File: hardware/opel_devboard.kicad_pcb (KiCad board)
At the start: 2 copper layers, 35 parts, among them P1 CONN_01X17, P2 CONN_01X06, P4 CONN_01X04, P5 CONN_01X04, SW1 SPST, SW2 SPST, U1 ISO1050, U2 LPC11C14, U3 MCP2515_TSSOP, U4 ISO1050, U5 MCP1755

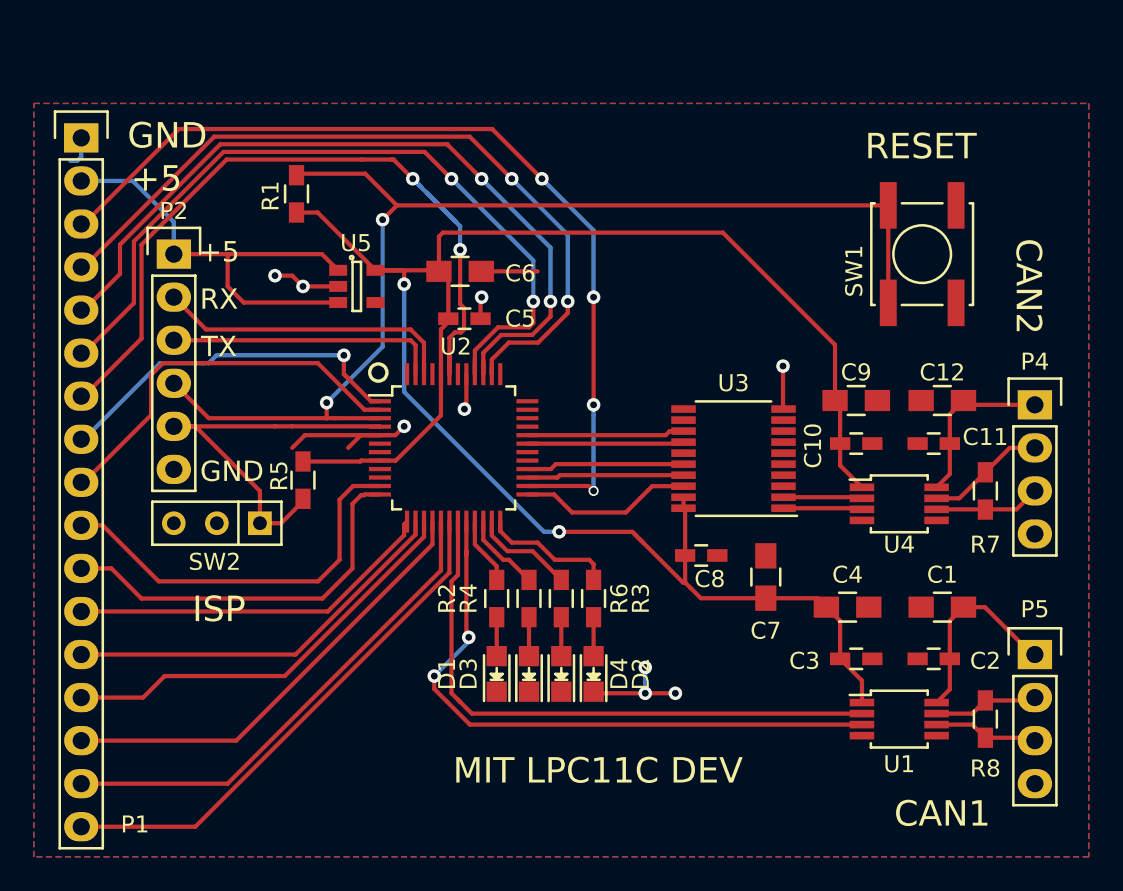
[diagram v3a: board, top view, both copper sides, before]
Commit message: devboard fixed, added LED, Added Capacitor, Changed CAN chips
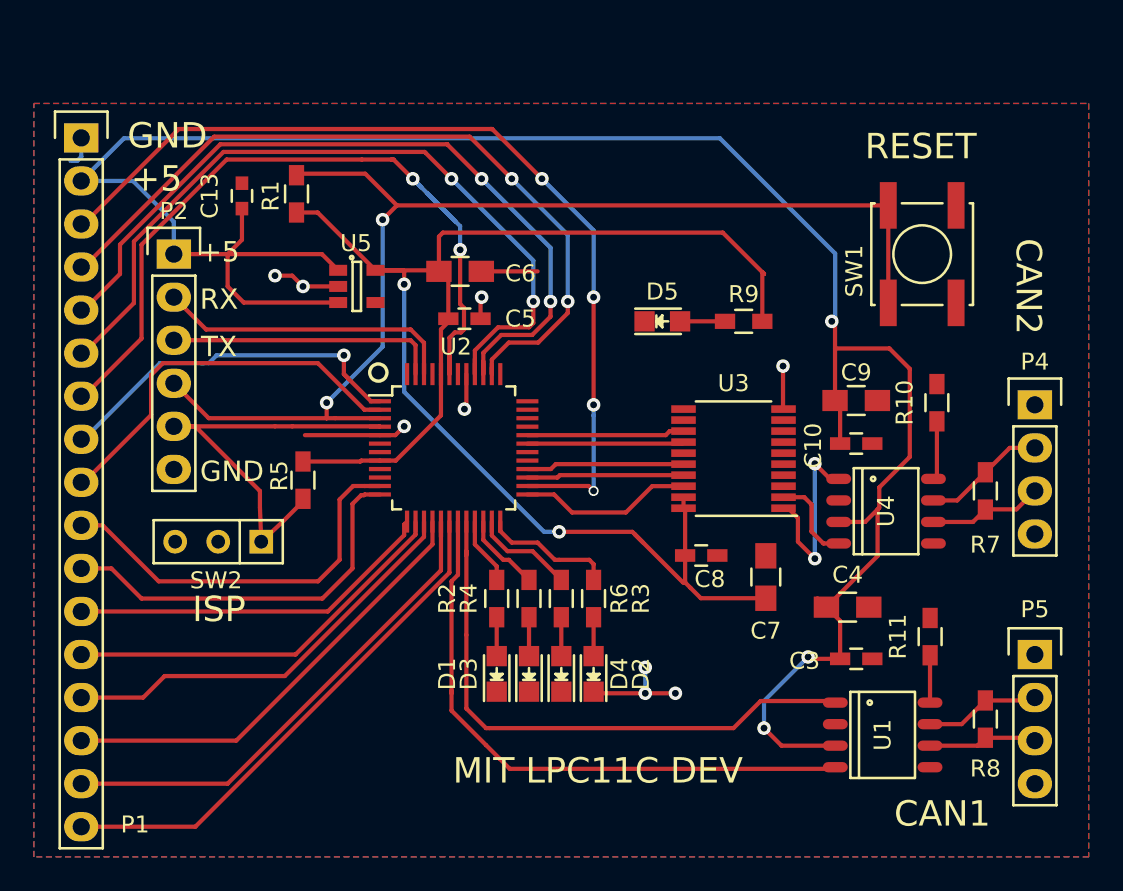
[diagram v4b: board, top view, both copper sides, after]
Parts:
- removed C1: 10uF, Capacitors_SMD:C_0805_HandSoldering
- removed C11, C2: 0.1uF, Capacitors_SMD:C_0603_HandSoldering
- removed C12: 1uF, Capacitors_SMD:C_0805_HandSoldering
- added C13: 1μF, Capacitors_SMD:C_0603, F.Cu at (165.9, 52.4)
- added D5: LED, LEDs:LED_0805, F.Cu at (190.7, 59.8)
- added R10: 20k, Resistors_SMD:R_0603_HandSoldering, F.Cu at (206.9, 64.6)
- added R11: 20k, Resistors_SMD:R_0603_HandSoldering, F.Cu at (206.5, 78.4)
- added R9: 200, Resistors_SMD:R_0603_HandSoldering, F.Cu at (195.5, 59.8)
- U1, U4: value ISO1050 -> MCP2551-I/SN; footprint Housings_SSOP:MSOP-8_3x3mm_Pitch0.65mm -> SO-8
- moved U1 1.35 mm to (203.7, 84.2), turned to 270 degrees
- moved SW2 1.09 mm to (164.5, 72.8)
- moved U4 0.89 mm to (203.9, 71.0), turned to 270 degrees
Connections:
- net GNDD renamed Net-(U1-Pad5)
- C10 pad 1: +3V3 -> +5V
- C3 pad 1: +3V3 -> +5V
- C4 pad 1: +3V3 -> +5V
- C9 pad 1: +3V3 -> +5V
- P4 pad 1: /Micro Controller/CAN2P -> /Output Connectors/CAN2P
- P5 pad 1: /Micro Controller/CAN1P -> /Output Connectors/CAN1P
- U1 pad 1: +3V3 -> Net-(U1-Pad1)
- U1 pad 2: Net-(U1-Pad2) -> GND
- U1 pad 3: Net-(U1-Pad3) -> +5V
- U1 pad 4: GND -> Net-(U1-Pad4)
- U1 pad 8: /Micro Controller/CAN1P -> Net-(R11-Pad1)
- U2 pad 19: Net-(U1-Pad2) -> Net-(U1-Pad4)
- U2 pad 20: Net-(U1-Pad3) -> Net-(U1-Pad1)
- U4 pad 1: +3V3 -> Net-(U3-Pad1)
- U4 pad 2: Net-(U3-Pad2) -> GND
- U4 pad 3: Net-(U3-Pad1) -> +5V
- U4 pad 4: GND -> Net-(U3-Pad2)
- U4 pad 5: GND -> Net-(U4-Pad5)
- U4 pad 8: /Micro Controller/CAN2P -> Net-(R10-Pad1)
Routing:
- net +5V: track 27.4 -> 129.9 mm, vias 0 -> 3
- net Net-(U1-Pad3): track 37.3 -> 0.00 mm, vias 2 -> 0
- net Net-(U1-Pad4): track 0.00 -> 35.6 mm
- net Net-(U1-Pad2): track 35.3 -> 0.00 mm
- net Net-(U1-Pad1): track 0.00 -> 34.2 mm
- net +3V3: track 116.9 -> 94.7 mm
- net /Micro Controller/CAN1P: track 11.7 -> 0.00 mm
- net /Micro Controller/CAN2P: track 10.1 -> 0.00 mm
- net Net-(U3-Pad1): track 4.66 -> 11.3 mm, vias 0 -> 2
- net Net-(R10-Pad1): track 0.00 -> 3.48 mm
- net GND: track 30.8 -> 27.6 mm
- net Net-(R11-Pad1): track 0.00 -> 2.80 mm
- net Net-(D5-Pad2): track 0.00 -> 2.65 mm
- net /Input Connectors/MCU_PROG_N: track 24.1 -> 25.5 mm
- net Net-(U3-Pad2): track 4.66 -> 5.32 mm
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
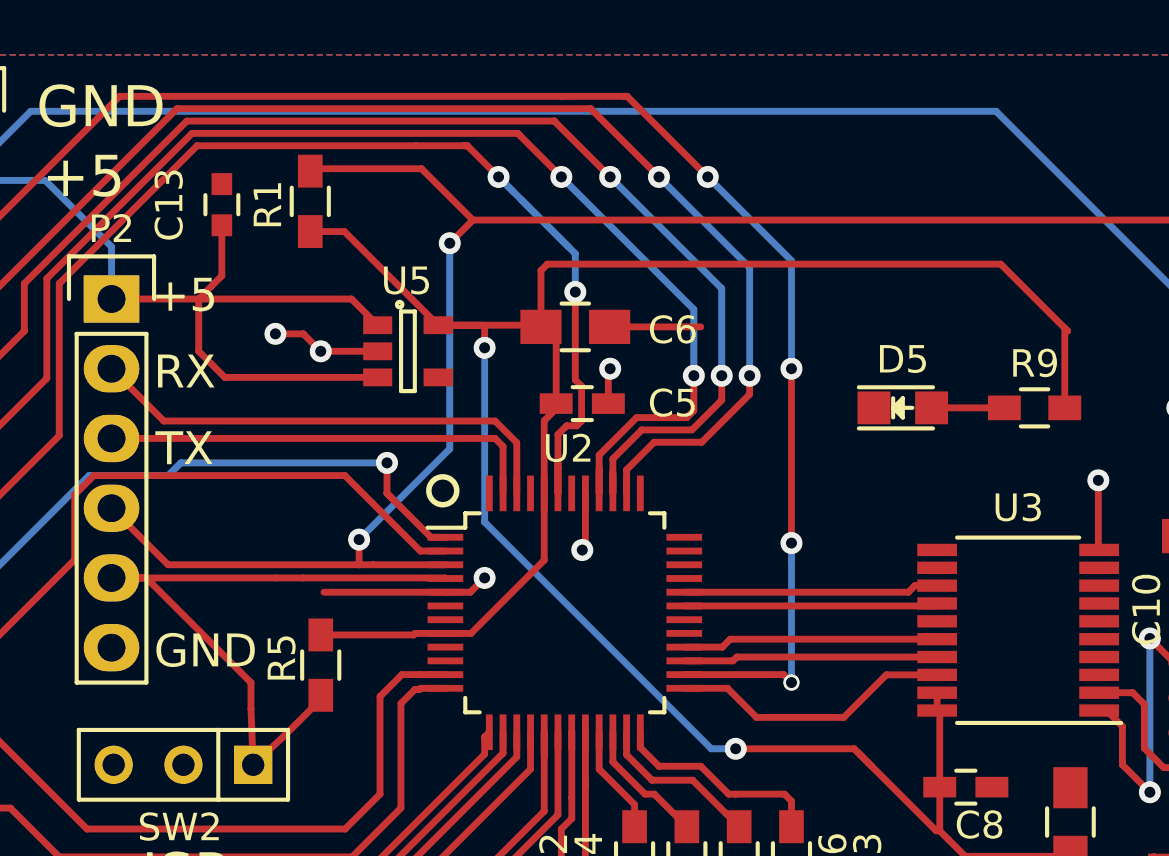
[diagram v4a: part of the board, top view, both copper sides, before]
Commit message: Changed to add a 3.3 volt connection
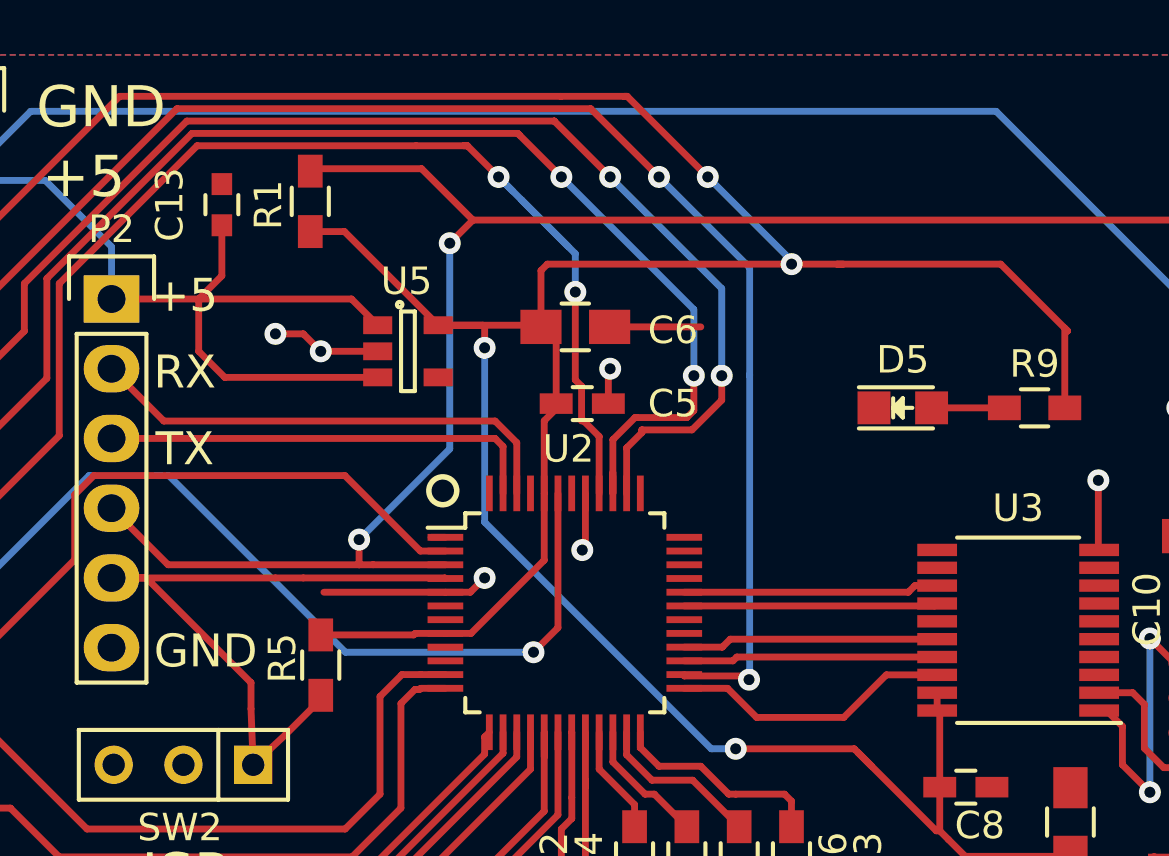
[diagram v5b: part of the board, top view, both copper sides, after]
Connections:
- P1 pad 3: /Micro Controller/PIO2_2 -> +3V3
- P1 pad 4: /Micro Controller/PIO2_3 -> /Micro Controller/PIO2_2
- P1 pad 5: /Micro Controller/PIO1_3 -> /Micro Controller/PIO2_3
- P1 pad 6: /Micro Controller/PIO1_4 -> /Micro Controller/PIO1_3
- P1 pad 7: /Micro Controller/PIO3_2 -> /Micro Controller/PIO1_4
- P1 pad 8: /Micro Controller/PIO2_6 -> /Micro Controller/PIO3_2
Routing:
- net +3V3: track 94.7 -> 130.1 mm, vias 2 -> 4
- net /Micro Controller/PIO2_6: track 22.0 -> 0.53 mm, vias 1 -> 0
- net /Micro Controller/PIO3_2: track 46.8 -> 31.7 mm, vias 2 -> 1
- net /Micro Controller/PIO2_2: track 54.5 -> 51.8 mm, vias 4 -> 2
- net /Micro Controller/PIO1_4: track 46.5 -> 45.4 mm
- net /Micro Controller/PIO2_3: track 45.8 -> 45.3 mm
